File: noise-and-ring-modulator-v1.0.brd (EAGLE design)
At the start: 33 x 17.8 mm, 72 parts, among them IC1 TL074JT, IC2 TL072JT, T1 NOISE-2N3904, U1 MC1496DR2G

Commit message: Fixed silk screen noise/ringmod
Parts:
- removed U$3: (no value), joakim:XONIK_LOGO_18

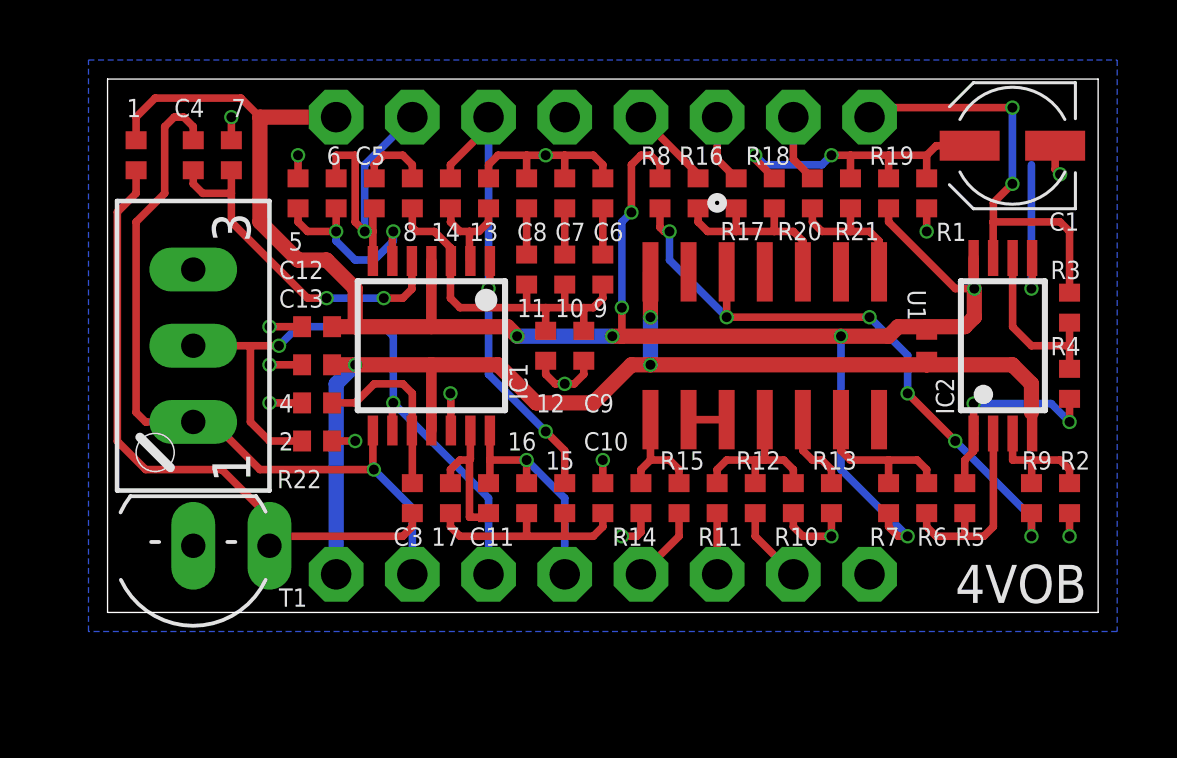
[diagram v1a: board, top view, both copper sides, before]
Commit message: Tiny silk screen fix
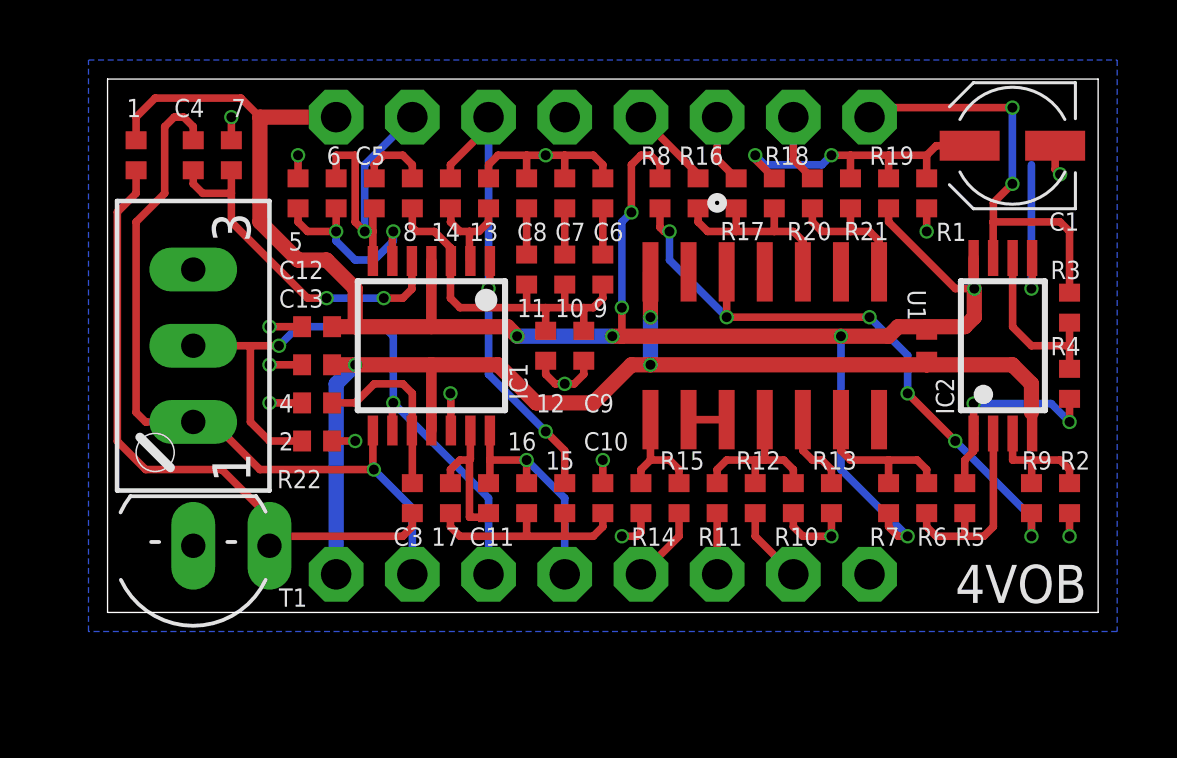
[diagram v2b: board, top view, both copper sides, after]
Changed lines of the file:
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@@
 <layer number="14" name="Route14" color="1" fill="6" visible="no" active="no"/>
 <layer number="15" name="Route15" color="4" fill="6" visible="no" active="no"/>
-<layer number="16" name="Bottom" color="1" fill="1" visible="yes" active="yes"/>
+<layer number="16" name="Bottom" color="1" fill="1" visible="no" active="yes"/>
 <layer number="17" name="Pads" color="2" fill="1" visible="yes" active="yes"/>
 <layer number="18" name="Vias" color="2" fill="1" visible="yes" active="yes"/>
@@
 <layer number="24" name="bOrigins" color="15" fill="1" visible="no" active="yes"/>
 <layer number="25" name="tNames" color="7" fill="1" visible="yes" active="yes"/>
-<layer number="26" name="bNames" color="7" fill="1" visible="yes" active="yes"/>
+<layer number="26" name="bNames" color="7" fill="1" visible="no" active="yes"/>
 <layer number="27" name="tValues" color="7" fill="1" visible="no" active="yes"/>
 <layer number="28" name="bValues" color="7" fill="1" visible="no" active="yes"/>
@@
 </element>
 <element name="R14" library="rcl" library_urn="urn:adsk.eagle:library:334" package="R0402" package3d_urn="urn:adsk.eagle:package:23547/3" value="2k7" x="17.78" y="3.81" smashed="yes" rot="R90">
-<attribute name="NAME" x="16.8275" y="2.2225" size="0.6096" layer="25" font="vector"/>
+<attribute name="NAME" x="17.4625" y="2.2225" size="0.6096" layer="25" font="vector"/>
 <attribute name="POPULARITY" value="0" x="17.78" y="3.81" size="1.778" layer="27" rot="R90" display="off"/>
 <attribute name="SPICEPREFIX" value="R" x="17.78" y="3.81" size="1.778" layer="27" rot="R90" display="off"/>
@@
 </element>
 <element name="R20" library="rcl" library_urn="urn:adsk.eagle:library:334" package="R0402" package3d_urn="urn:adsk.eagle:package:23547/3" value="12k" x="23.495" y="13.97" smashed="yes" rot="R90">
-<attribute name="NAME" x="23.8125" y="13.0175" size="0.6096" layer="25" font="vector" rot="R180"/>
+<attribute name="NAME" x="24.13" y="13.0175" size="0.6096" layer="25" font="vector" rot="R180"/>
 <attribute name="POPULARITY" value="0" x="23.495" y="13.97" size="1.778" layer="27" rot="R90" display="off"/>
 <attribute name="SPICEPREFIX" value="R" x="23.495" y="13.97" size="1.778" layer="27" rot="R90" display="off"/>
@@
 </element>
 <element name="R21" library="rcl" library_urn="urn:adsk.eagle:library:334" package="R0402" package3d_urn="urn:adsk.eagle:package:23547/3" value="2k7" x="24.765" y="13.97" smashed="yes" rot="R90">
-<attribute name="NAME" x="25.7175" y="13.0175" size="0.6096" layer="25" font="vector" rot="R180"/>
+<attribute name="NAME" x="26.035" y="13.0175" size="0.6096" layer="25" font="vector" rot="R180"/>
 <attribute name="POPULARITY" value="0" x="24.765" y="13.97" size="1.778" layer="27" rot="R90" display="off"/>
 <attribute name="SPICEPREFIX" value="R" x="24.765" y="13.97" size="1.778" layer="27" rot="R90" display="off"/>
@@
 </element>
 <element name="R18" library="rcl" library_urn="urn:adsk.eagle:library:334" package="R0402" package3d_urn="urn:adsk.eagle:package:23547/3" value="2k7" x="22.225" y="13.97" smashed="yes" rot="R90">
-<attribute name="NAME" x="21.2725" y="14.9225" size="0.6096" layer="25" font="vector"/>
+<attribute name="NAME" x="21.9075" y="14.9225" size="0.6096" layer="25" font="vector"/>
 <attribute name="POPULARITY" value="0" x="22.225" y="13.97" size="1.778" layer="27" rot="R90" display="off"/>
 <attribute name="SPICEPREFIX" value="R" x="22.225" y="13.97" size="1.778" layer="27" rot="R90" display="off"/>

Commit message: Replaced pin footprints
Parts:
- removed PINK, RED, WHITE, X1, X10, X2, X20, X21, X22, X3, X4, X5, X6, X7, X8, X9: (no value), joakim:MA01N-1J
- added X11, X12: (no value), joakim:MA08N-1J
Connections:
- net +12V: now also X12.8; no longer X1.1
- net -12V: now also X11.1; no longer X3.1
- net CARRIER: now also X12.4; no longer X7.1
- net CAR_TRIM_1: now also X12.3; no longer X9.1
- net CAR_TRIM_2: now also X12.2; no longer X8.1
- net GND: now also X12.5; no longer X2.1
- net LEV1: now also X11.3; no longer X20.1
- net LEV2: now also X11.2; no longer X22.1
- net OUT: now also X12.1; no longer X10.1
- net PINK: now also X12.6; no longer PINK.1
- net RED: now also X11.4; no longer RED.1
- net SIGNAL: now also X11.7; no longer X6.1
- net SIG_TRIM_1: now also X11.6; no longer X5.1
- net SIG_TRIM_2: now also X11.5; no longer X4.1
- net WHITE: now also X12.7; no longer WHITE.1
